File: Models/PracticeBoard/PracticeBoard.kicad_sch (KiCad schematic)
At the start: 0 parts

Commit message: Elaborated more on the board
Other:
- added sheet Chip1 (Chip1.kicad_sch)
- note added: "Lay out the footprint for Chip1 on the PCB, calculate board space, then decide how many copies to include."
- note added: "TBD number of through holes, 10 0805 resistors We do need THT practice, to test the efficacy of the cheap solder sucker. For every practice board, solder the THT parts, then desolder them, then assemble the SMT parts."
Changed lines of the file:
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@@
 	(generator_version "9.0")
 	(paper "A4")
+	(text "TBD number of through holes, 10 0805 resistors\n\nWe do need THT practice, to test the efficacy\nof the cheap solder sucker. For every practice\nboard, solder the THT parts, then desolder them,\nthen assemble the SMT parts."
+		(exclude_from_sim no)
+		(at 77.216 27.178 0)
+		(effects
+			(font
+				(size 1.27 1.27)
+			)
+			(justify left top)
+		)
+	)
+	(text "Lay out the footprint for Chip1 on the PCB, \ncalculate board space,\nthen decide how many copies to include."
+		(exclude_from_sim no)
+		(at 127.508 76.708 0)
+		(effects
+			(font
+				(size 1.27 1.27)
+			)
+			(justify left top)
+		)
+	)
+	(sheet
+		(at 76.2 76.2)
+		(size 38.1 25.4)
+		(exclude_from_sim no)
+		(in_bom yes)
+		(on_board yes)
+		(dnp no)
+		(fields_autoplaced yes)
+		(stroke
+			(width 0.1524)
+			(type solid)
+		)
+		(fill
+			(color 0 0 0 0.0000)
+		)
+		(property "Sheetname" "Chip1"
+			(at 76.2 75.4884 0)
+			(effects
+				(font
+					(size 1.27 1.27)
+				)
+				(justify left bottom)
+			)
+		)
+		(property "Sheetfile" "Chip1.kicad_sch"
+			(at 76.2 102.1846 0)
+			(effects
+				(font
+					(size 1.27 1.27)
+				)
+				(justify left top)
+			)
+		)
+		(instances
+			(project "PracticeBoard"
+				(path "/424a2905-d6ee-47e0-a55f-41cae3b03774"
+					(page "2")
+				)
+			)
+		)
+	)
 	(sheet_instances
 		(path "/"

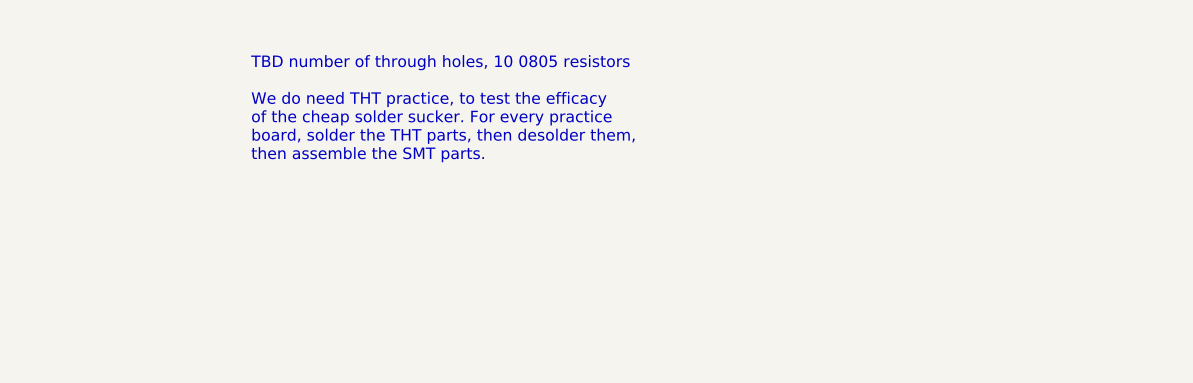
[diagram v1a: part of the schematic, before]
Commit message: Going to practice laying out the resistors near a chip, although the annotations will likely be overwritten later, requiring a duplication of the work for PCB layout
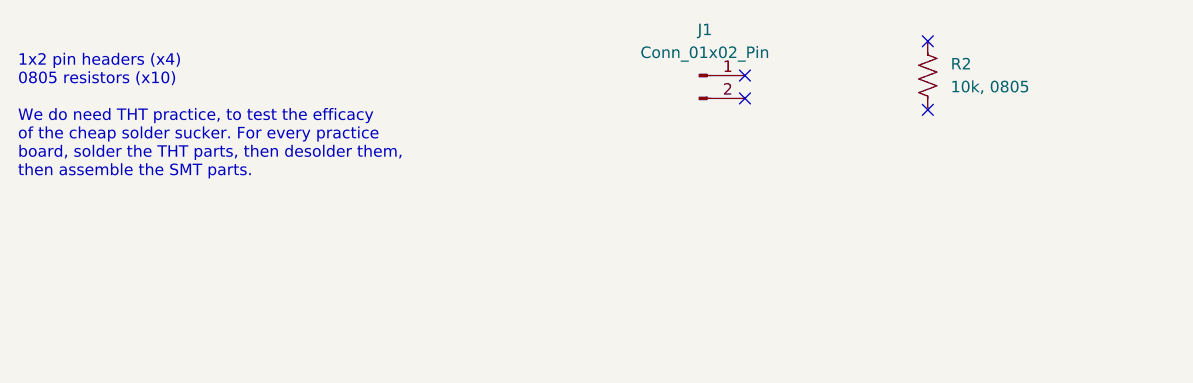
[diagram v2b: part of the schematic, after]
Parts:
- added J1: Conn_01x02_Pin, symbol Connector:Conn_01x02_Pin
- added R2: 10k, 0805, symbol Device:R_US
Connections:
- no-connect marks 0 -> 4
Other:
- note added: "1x2 pin headers (x4) 0805 resistors (x10) We do need THT practice, to test the efficacy of the cheap solder sucker. For every practice board, solder the THT parts, then desolder them, then assemble the SMT parts."
- note removed: "TBD number of through holes, 10 0805 resistors We do need THT practice, to test the efficacy of the cheap solder sucker. For every practice board, solder the THT parts, then desolder them, then assemble the SMT parts."
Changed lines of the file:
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@@
 	(generator_version "9.0")
 	(paper "A4")
-	(text "TBD number of through holes, 10 0805 resistors\n\nWe do need THT practice, to test the efficacy\nof the cheap solder sucker. For every practice\nboard, solder the THT parts, then desolder them,\nthen assemble the SMT parts."
-		(exclude_from_sim no)
-		(at 77.216 27.178 0)
+	(text "1x2 pin headers (x4)\n0805 resistors (x10)\n\nWe do need THT practice, to test the efficacy\nof the cheap solder sucker. For every practice\nboard, solder the THT parts, then desolder them,\nthen assemble the SMT parts."
+		(exclude_from_sim no)
+		(at 51.308 26.924 0)
 		(effects
 			(font
@@
 		)
 	)
+	(no_connect
+		(at 152.4 33.02)
+	)
+	(no_connect
+		(at 132.08 31.75)
+	)
+	(no_connect
+		(at 152.4 25.4)
+	)
+	(no_connect
+		(at 132.08 29.21)
+	)
+	(symbol
+		(lib_id "Connector:Conn_01x02_Pin")
+		(at 127 29.21 0)
+		(unit 1)
+		(exclude_from_sim no)
+		(in_bom yes)
+		(on_board yes)
+		(dnp no)
+		(fields_autoplaced yes)
+		(property "Reference" "J1"
+			(at 127.635 24.13 0)
+			(effects
+				(font
+					(size 1.27 1.27)
+				)
+			)
+		)
+		(property "Value" "Conn_01x02_Pin"
+			(at 127.635 26.67 0)
+			(effects
+				(font
+					(size 1.27 1.27)
+				)
+			)
+		)
+		(property "Footprint" ""
+			(at 127 29.21 0)
+			(effects
+				(font
+					(size 1.27 1.27)
+				)
+				(hide yes)
+			)
+		)
+		(property "Datasheet" "~"
+			(at 127 29.21 0)
+			(effects
+				(font
+					(size 1.27 1.27)
+				)
+				(hide yes)
+			)
+		)
+		(property "Description" "Generic connector, single row, 01x02, script generated"
+			(at 127 29.21 0)
+			(effects
+				(font
+					(size 1.27 1.27)
+				)
+				(hide yes)
+			)
+		)
+		(pin "1"
+		)
+		(pin "2"
+		)
+		(instances
+			(project ""
+				(path "/424a2905-d6ee-47e0-a55f-41cae3b03774"
+					(reference "J1")
+					(unit 1)
+				)
+			)
+		)
+	)
+	(symbol
+		(lib_id "Device:R_US")
+		(at 152.4 29.21 0)
+		(unit 1)
+		(exclude_from_sim no)
+		(in_bom yes)
+		(on_board yes)
+		(dnp no)
+		(fields_autoplaced yes)
+		(property "Reference" "R2"
+			(at 154.94 27.9399 0)
+			(effects
+				(font
+					(size 1.27 1.27)
+				)
+				(justify left)
+			)
+		)
+		(property "Value" "10k, 0805"
+			(at 154.94 30.4799 0)
+			(effects
+				(font
+					(size 1.27 1.27)
+				)
+				(justify left)
+			)
+		)
+		(property "Footprint" ""
+			(at 153.416 29.464 90)
+			(effects
+				(font
+					(size 1.27 1.27)
+				)
+				(hide yes)
+			)
+		)
+		(property "Datasheet" "~"
+			(at 152.4 29.21 0)
+			(effects
+				(font
+					(size 1.27 1.27)
+				)
+				(hide yes)
+			)
+		)
+		(property "Description" "Resistor, US symbol"
+			(at 152.4 29.21 0)
+			(effects
+				(font
+					(size 1.27 1.27)
+				)
+				(hide yes)
+			)
+		)
+		(property "Purchase Link" "https://www.digikey.com/en/products/detail/vishay-dale/CRCW080510K0JNEA/1175222"
+			(at 152.4 29.21 0)
+			(effects
+				(font
+					(size 1.27 1.27)
+				)
+				(hide yes)
+			)
+		)
+		(property "Cost" "$0.10"
+			(at 152.4 29.21 0)
+			(effects
+				(font
+					(size 1.27 1.27)
+				)
+				(hide yes)
+			)
+		)
+		(property "RoHS Compliant" "YES"
+			(at 152.4 29.21 0)
+			(effects
+				(font
+					(size 1.27 1.27)
+				)
+				(hide yes)
+			)
+		)
+		(property "Cost (qty10)" "$0.035"
+			(at 152.4 29.21 0)
+			(effects
+				(font
+					(size 1.27 1.27)
+				)
+				(hide yes)
+			)
+		)
+		(pin "2"
+		)
+		(pin "1"
+		)
+		(instances
+			(project ""
+				(path "/424a2905-d6ee-47e0-a55f-41cae3b03774"
+					(reference "R2")
+					(unit 1)
+				)
+			)
+		)
+	)

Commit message: Rough sketch of the layout resulted in a calculated price of
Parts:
- J1: footprint (none) -> Connector_Custom:PinHeader_1x2
- R2: footprint (none) -> TwoTerminal:RESC0805
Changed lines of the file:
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@@
 			)
 		)
-		(property "Footprint" ""
+		(property "Footprint" "Connector_Custom:PinHeader_1x2"
 			(at 127 29.21 0)
 			(effects
@@
 			)
 		)
-		(property "Footprint" ""
+		(property "Footprint" "TwoTerminal:RESC0805"
 			(at 153.416 29.464 90)
 			(effects

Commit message: Finally settled on the relative layout of all parts on the board
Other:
- note added: "1x2 pin headers (x6) 0805 resistors (x12) We do need THT practice, to test the efficacy of the cheap solder sucker. For every practice board, solder the THT parts, then desolder them, then assemble the SMT parts."
- note removed: "1x2 pin headers (x4) 0805 resistors (x10) We do need THT practice, to test the efficacy of the cheap solder sucker. For every practice board, solder the THT parts, then desolder them, then assemble the SMT parts."
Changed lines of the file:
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@@
 	(generator_version "9.0")
 	(paper "A4")
-	(text "1x2 pin headers (x4)\n0805 resistors (x10)\n\nWe do need THT practice, to test the efficacy\nof the cheap solder sucker. For every practice\nboard, solder the THT parts, then desolder them,\nthen assemble the SMT parts."
+	(text "1x2 pin headers (x6)\n0805 resistors (x12)\n\nWe do need THT practice, to test the efficacy\nof the cheap solder sucker. For every practice\nboard, solder the THT parts, then desolder them,\nthen assemble the SMT parts."
 		(exclude_from_sim no)
 		(at 51.308 26.924 0)

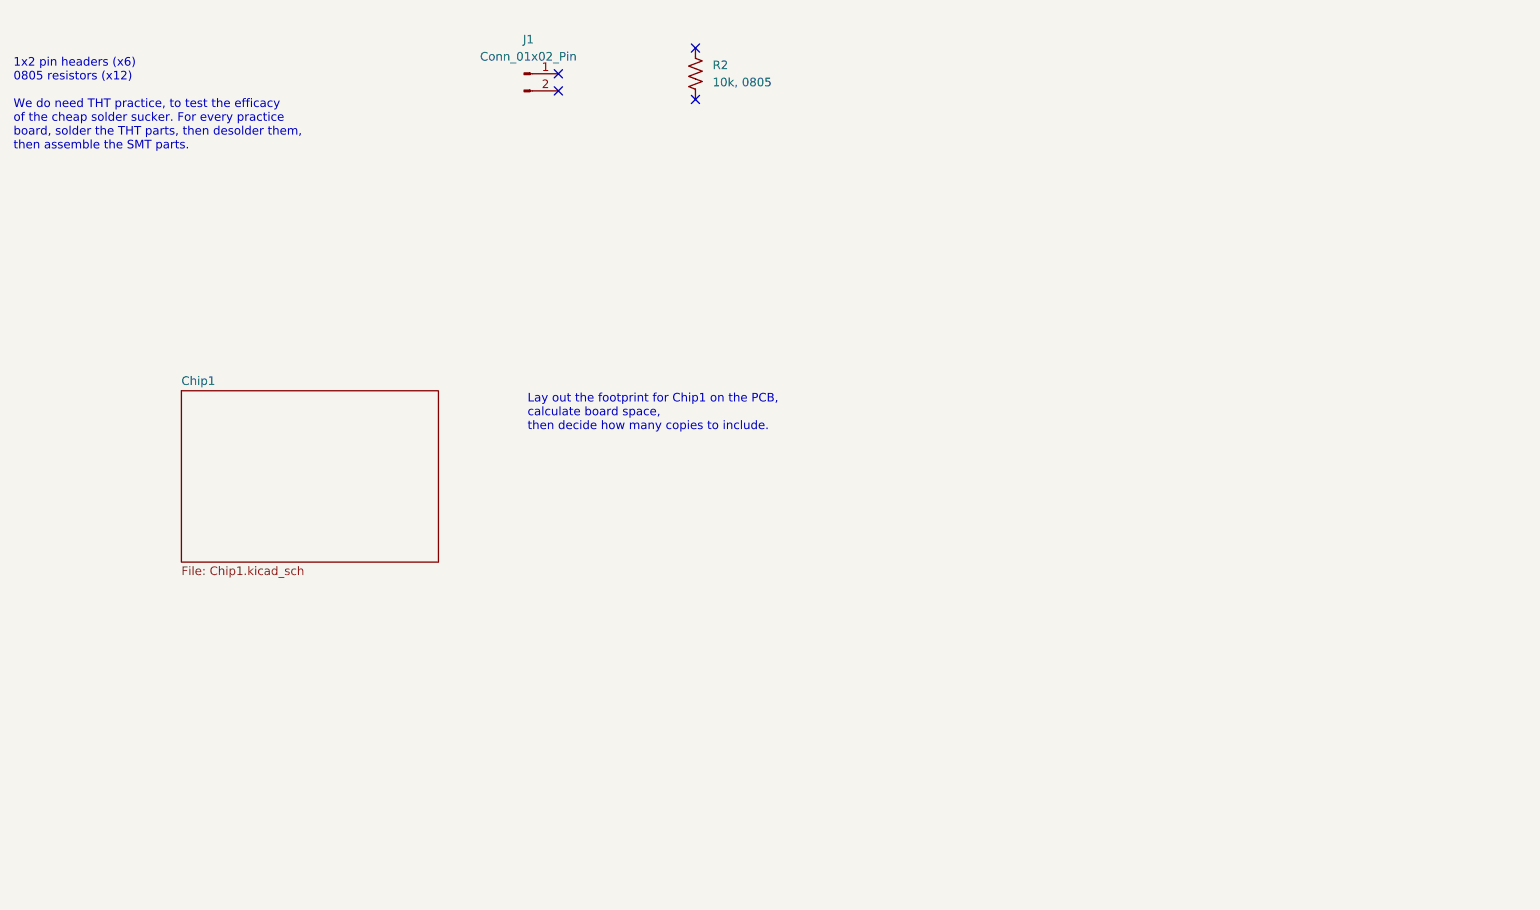
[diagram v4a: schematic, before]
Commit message: Finished the schematic for the practice board
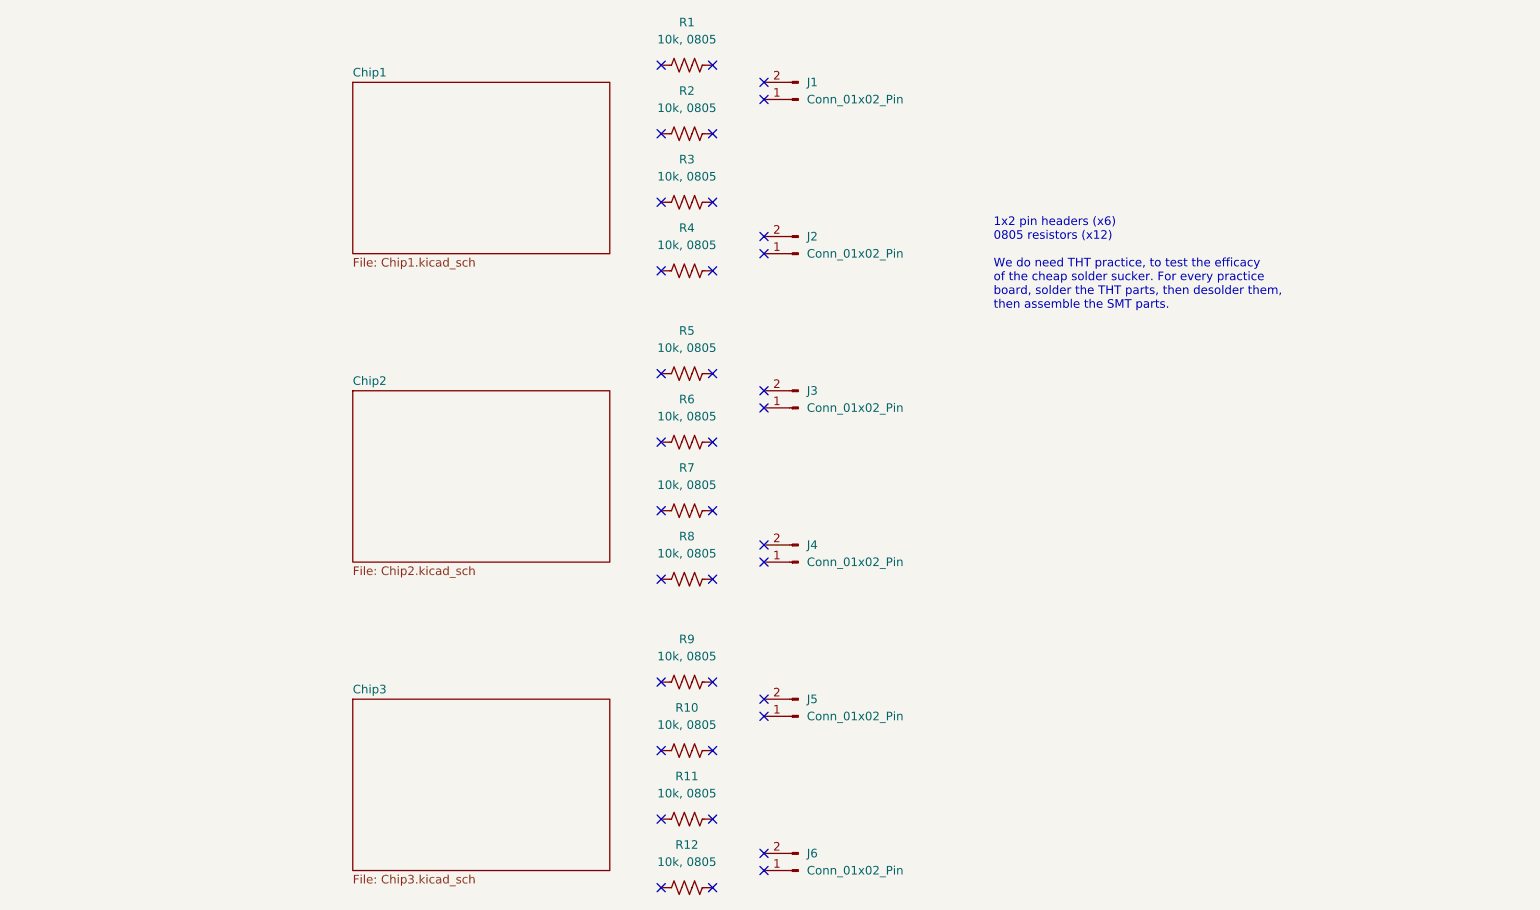
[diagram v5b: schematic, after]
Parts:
- added J2, J3, J4, J5, J6: Conn_01x02_Pin, Connector_Custom:PinHeader_1x2, symbol Connector:Conn_01x02_Pin
- added R10, R11, R12, R2, R3, R4, R5, R6, R7, R8, R9: 10k, 0805, TwoTerminal:RESC0805, symbol Device:R_US
- renumbered R2 to R1
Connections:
- no-connect marks 4 -> 36
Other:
- added sheet Chip2 (Chip2.kicad_sch)
- added sheet Chip3 (Chip3.kicad_sch)
- note removed: "Lay out the footprint for Chip1 on the PCB, calculate board space, then decide how many copies to include."
- moved on the sheet: J1, R1

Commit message: Finished the layout of the practice board
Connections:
- net GND: now reaches J6.1 (Pin_1)
- net GND: now also J4.1 (Pin_1), J4.2 (Pin_2), J5.1 (Pin_1), J5.2 (Pin_2), J6.2 (Pin_2), R10.1, R10.2, R11.1, R11.2, R12.1, R12.2, R7.1, R7.2, R8.1, R8.2, R9.1, R9.2
- no-connect marks 36 -> 18
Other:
- moved on the sheet: J1, J2, J3, J4, J5, J6, R1, R10, R11, R12, R2, R3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
